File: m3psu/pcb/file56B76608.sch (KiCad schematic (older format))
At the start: 48 parts

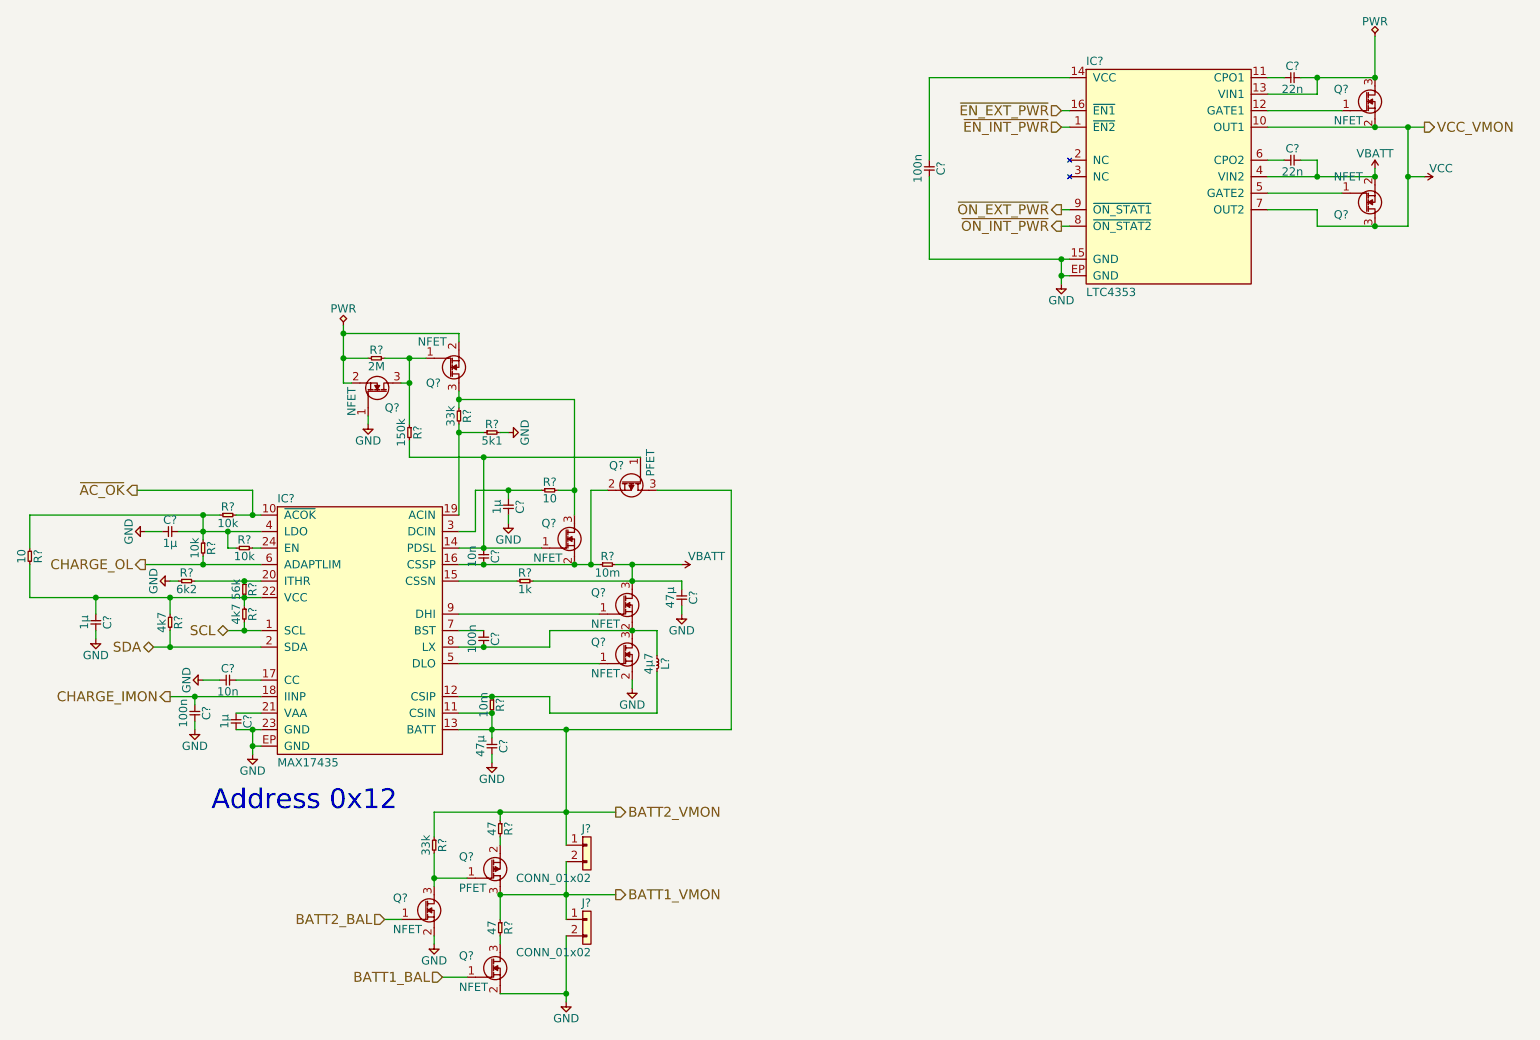
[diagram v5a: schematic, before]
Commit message: Added current monitor and control for pyros. Modified DC/DC converters.
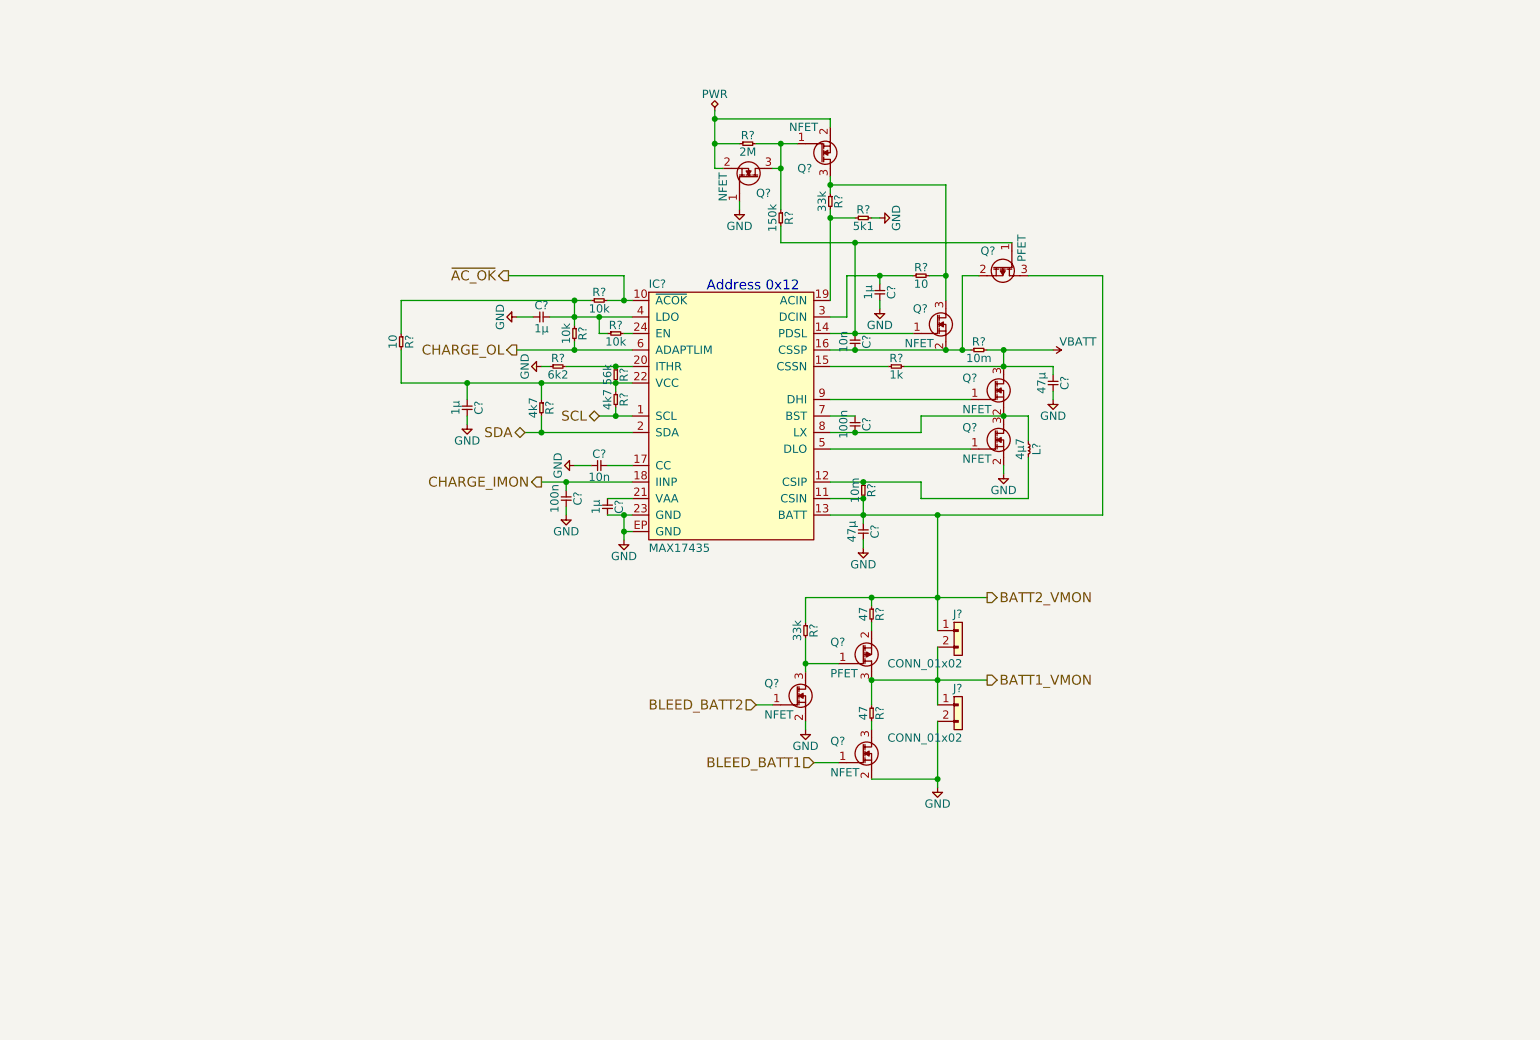
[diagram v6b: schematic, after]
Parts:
- removed C?: 100n, agg:0402, symbol C
- removed C?: 22n, ag:0402, symbol C
- removed C?: 22n, agg:0402, symbol C
- removed IC?: LTC4353, agg:DFN-16-EP-LTC-DE, symbol LTC4353
- removed Q? (x2): NFET, symbol NFET
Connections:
- net BATT1_BAL renamed BLEED_BATT1
- net BATT2_BAL renamed BLEED_BATT2
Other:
- moved on the sheet: C?, IC?, J?, L?, Q?, R?

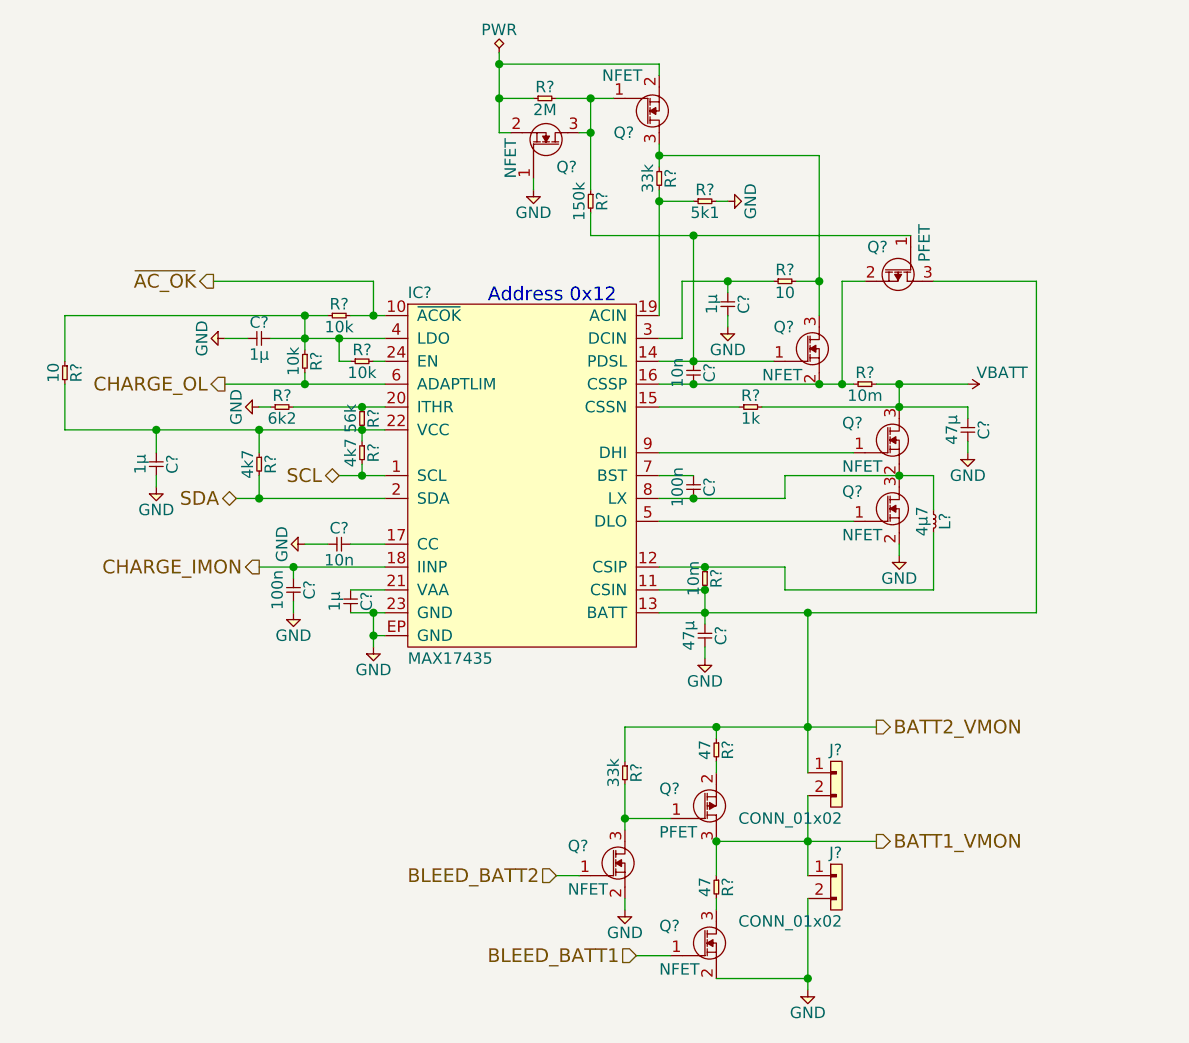
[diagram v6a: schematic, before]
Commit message: Changes in arrangement of schematic. Started wiring interconnects. WIP.
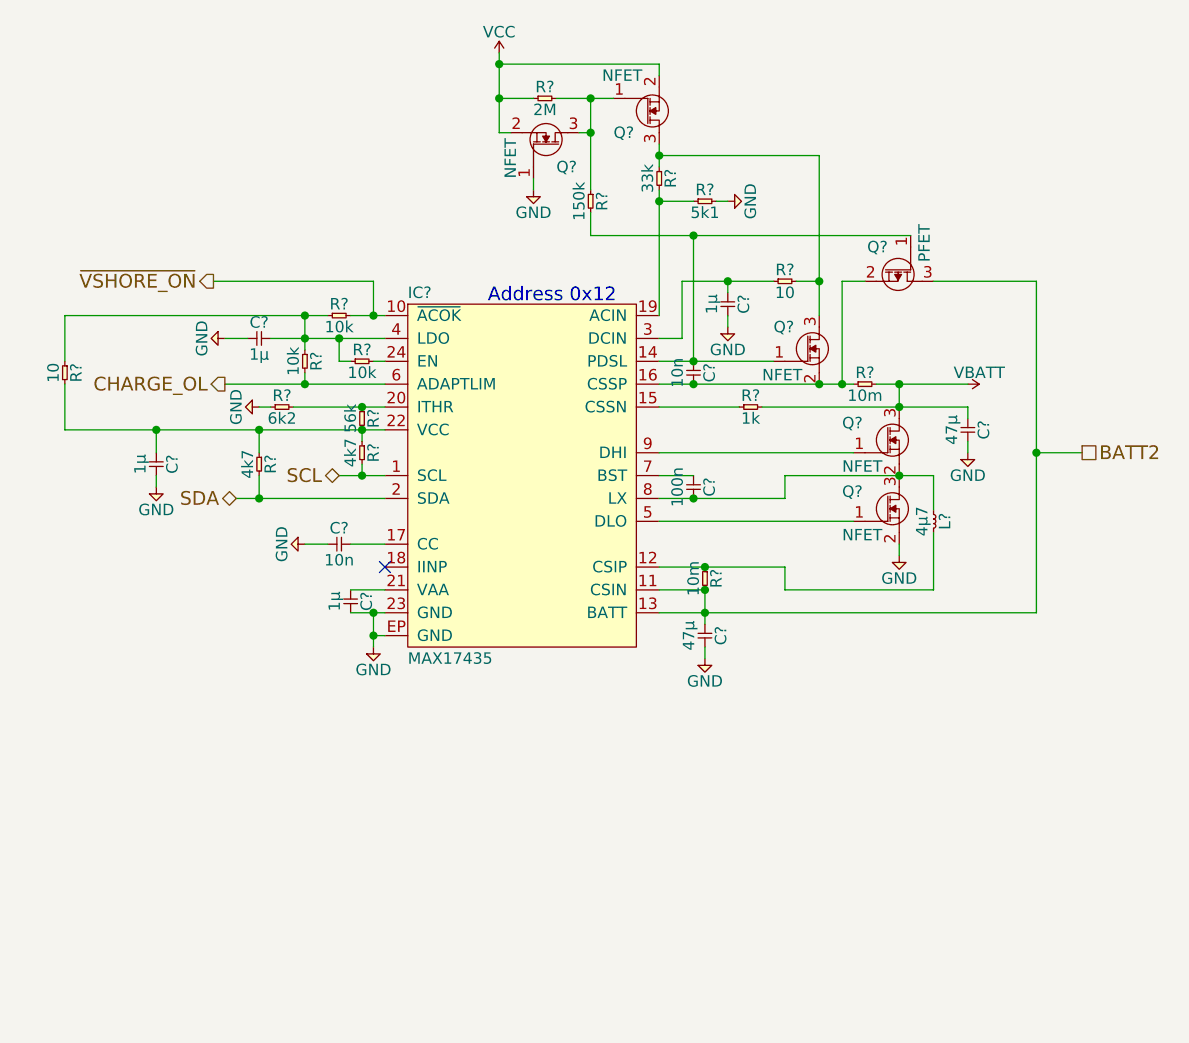
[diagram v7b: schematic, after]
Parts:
- removed C?: 100n, agg:0402, symbol C
- removed J? (x2): CONN_01x02, symbol CONN_01x02
- removed Q?: PFET, symbol PFET
- removed Q? (x2): NFET, symbol NFET
- removed R? (x2): 47, agg:0805, symbol R
- removed R?: 33k, agg:0402, symbol R
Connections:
- net VCC: now reaches Q?.2 (S), Q?.2 (S), R?.1
- net BATT2_VMON renamed BATT2
- net CHARGE_IMON: no longer names the net of IC?.18 (IINP)
- net ~AC_OK renamed ~VSHORE_ON
- no-connect marks 0 -> 1
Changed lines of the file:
@@
 $Descr A4 11693 8268
 encoding utf-8
-Sheet 3 12
+Sheet 3 13
 Title ""
 Date ""
@@
 $EndDescr
 $Comp
-L CONN_01x02 J?
-U 1 1 56B94890
-P 7200 4800
-F 0 "J?" H 7150 4900 50  0000 L CNN
-F 1 "CONN_01x02" H 7150 4600 50  0000 L CNN
-F 2 "" H 7200 4800 50  0001 C CNN
-F 3 "" H 7200 4800 50  0001 C CNN
-	1    7200 4800
-	-1   0    0    -1
-$EndComp
-$Comp
-L CONN_01x02 J?
-U 1 1 56B9491D
-P 7200 5250
-F 0 "J?" H 7150 5350 50  0000 L CNN
-F 1 "CONN_01x02" H 7150 5050 50  0000 L CNN
-F 2 "" H 7200 5250 50  0001 C CNN
-F 3 "" H 7200 5250 50  0001 C CNN
-	1    7200 5250
-	-1   0    0    -1
-$EndComp
-$Comp
 L MAX17435 IC?
 U 1 1 56B94994
@@
 $EndComp
 $Comp
-L GND #PWR08
-U 1 1 56B94BFC
-P 7100 5750
-F 0 "#PWR08" H 6970 5790 50  0001 L CNN
-F 1 "GND" H 7100 5650 50  0000 C CNN
-F 2 "" H 7100 5750 60  0000 C CNN
-F 3 "" H 7100 5750 60  0000 C CNN
-	1    7100 5750
-	1    0    0    -1
-$EndComp
-$Comp
 L R R?
 U 1 1 56B94FDE
@@
 F 4 "2210793" H 5000 3800 60  0001 C CNN "Farnell"
 	1    5000 3800
-	1    0    0    -1
-$EndComp
-$Comp
-L C C?
-U 1 1 56B99D2E
-P 4850 3950
-F 0 "C?" H 4900 4020 50  0000 C CNN
-F 1 "100n" H 4900 3880 50  0000 C CNN
-F 2 "agg:0402" H 4850 3950 50  0001 C CNN
-F 3 "" H 4850 3950 50  0001 C CNN
-F 4 "2496811" H 4850 3950 60  0001 C CNN "Farnell"
-	1    4850 3950
-	0    1    1    0
-$EndComp
-$Comp
-L GND #PWR013
-U 1 1 56B99D99
-P 4850 4100
-F 0 "#PWR013" H 4720 4140 50  0001 L CNN
-F 1 "GND" H 4850 4000 50  0000 C CNN
-F 2 "" H 4850 4100 60  0000 C CNN
-F 3 "" H 4850 4100 60  0000 C CNN
-	1    4850 4100
 	1    0    0    -1
 $EndComp
@@
 	1    0    0    -1
 $EndComp
-$Comp
-L VBATT #PWR019
-U 1 1 56C38460
-P 7800 3100
-F 0 "#PWR019" H 7800 3210 50  0001 L CNN
-F 1 "VBATT" V 7750 3250 50  0000 C CNN
-F 2 "" H 7800 3100 60  0000 C CNN
-F 3 "" H 7800 3100 60  0000 C CNN
-	1    7800 3100
-	0    1    1    0
-$EndComp
-$Comp
-L PFET Q?
-U 1 1 56C3D29E
-P 6700 4900
-F 0 "Q?" H 6450 4930 50  0000 L CNN
-F 1 "PFET" H 6450 4740 50  0000 L CNN
-F 2 "" H 6700 4900 50  0001 C CNN
-F 3 "" H 6700 4900 50  0001 C CNN
-F 4 "2335393" H 6700 4900 60  0001 C CNN "Farnell"
-	1    6700 4900
-	1    0    0    -1
-$EndComp
-$Comp
-L NFET Q?
-U 1 1 56C3D776
-P 6700 5500
-F 0 "Q?" H 6450 5530 50  0000 L CNN
-F 1 "NFET" H 6450 5340 50  0000 L CNN
-F 2 "" H 6700 5500 50  0001 C CNN
-F 3 "" H 6700 5500 50  0001 C CNN
-F 4 "2364070" H 6700 5500 60  0001 C CNN "Farnell"
-	1    6700 5500
-	1    0    0    -1
-$EndComp
 Text HLabel 4500 2650 0    60   Output ~ 0
-~AC_OK
+~VSHORE_ON
 Text HLabel 4550 3100 0    60   Output ~ 0
 CHARGE_OL
-Text HLabel 4700 3900 0    60   Output ~ 0
-CHARGE_IMON
 Text HLabel 5050 3500 0    60   BiDi ~ 0
 SCL
 Text HLabel 4600 3600 0    60   BiDi ~ 0
 SDA
-$Comp
-L R R?
-U 1 1 56C428FC
-P 6700 4650
-F 0 "R?" H 6750 4700 50  0000 C CNN
-F 1 "47" H 6750 4600 50  0000 C CNN
-F 2 "agg:0805" H 6700 4650 50  0001 C CNN
-F 3 "" H 6700 4650 50  0001 C CNN
-F 4 "1750737" H 6700 4650 60  0001 C CNN "Farnell"
-F 5 "0.5W" H 6700 4650 60  0001 C CNN "Power"
-	1    6700 4650
-	0    1    1    0
-$EndComp
-$Comp
-L R R?
-U 1 1 56C429C6
-P 6700 5250
-F 0 "R?" H 6750 5300 50  0000 C CNN
-F 1 "47" H 6750 5200 50  0000 C CNN
-F 2 "agg:0805" H 6700 5250 50  0001 C CNN
-F 3 "" H 6700 5250 50  0001 C CNN
-F 4 "1750737" H 6700 5250 60  0001 C CNN "Farnell"
-F 5 "0.5W" H 6700 5250 60  0001 C CNN "Power"
-	1    6700 5250
-	0    1    1    0
-$EndComp
-Text HLabel 6350 5600 0    60   Input ~ 0
-BLEED_BATT1
-Text HLabel 7400 5100 2    60   Output ~ 0
-BATT1_VMON
-Text HLabel 7400 4600 2    60   Output ~ 0
-BATT2_VMON
-$Comp
-L NFET Q?
-U 1 1 56C4464A
-P 6300 5150
-F 0 "Q?" H 6050 5180 50  0000 L CNN
-F 1 "NFET" H 6050 4990 50  0000 L CNN
-F 2 "" H 6300 5150 50  0001 C CNN
-F 3 "" H 6300 5150 50  0001 C CNN
-F 4 "2364070" H 6300 5150 60  0001 C CNN "Farnell"
-	1    6300 5150
-	1    0    0    -1
-$EndComp
-$Comp
-L GND #PWR020
-U 1 1 56C4477F
-P 6300 5400
-F 0 "#PWR020" H 6170 5440 50  0001 L CNN
-F 1 "GND" H 6300 5300 50  0000 C CNN
-F 2 "" H 6300 5400 60  0000 C CNN
-F 3 "" H 6300 5400 60  0000 C CNN
-	1    6300 5400
-	1    0    0    -1
-$EndComp
-$Comp
-L R R?
-U 1 1 56C44E02
-P 6300 4750
-F 0 "R?" H 6350 4800 50  0000 C CNN
-F 1 "33k" H 6350 4700 50  0000 C CNN
-F 2 "agg:0402" H 6300 4750 50  0001 C CNN
-F 3 "" H 6300 4750 50  0001 C CNN
-F 4 "2447160" H 6300 4750 60  0001 C CNN "Farnell"
-	1    6300 4750
-	0    1    1    0
-$EndComp
-Text HLabel 6000 5250 0    60   Input ~ 0
-BLEED_BATT2
-$Comp
-L PWR #FLG024
-U 1 1 56C61BF6
-P 5750 1650
-F 0 "#FLG024" H 5750 1810 50  0001 C CNN
-F 1 "PWR" H 5750 1750 50  0000 C CNN
-F 2 "" H 5750 1650 50  0001 C CNN
-F 3 "" H 5750 1650 50  0001 C CNN
-	1    5750 1650
-	1    0    0    -1
-$EndComp
+Text HLabel 8300 3400 2    60   UnSpc ~ 0
+BATT2
 $Comp
 L NFET Q?
@@
 Wire Wire Line
 	7250 2650 7350 2650
-Connection ~ 7100 4100
 Wire Wire Line
 	8100 4100 8100 2650
@@
 Connection ~ 5750 1700
 Wire Wire Line
-	6700 4650 6700 4600
-Wire Wire Line
-	7100 4100 7100 4800
-Wire Wire Line
 	6750 2650 6750 2700
 Wire Wire Line
@@
 	5150 3450 5150 3500
 Connection ~ 6600 3600
-Wire Wire Line
-	6100 5250 6000 5250
-Connection ~ 6300 5000
-Connection ~ 6700 4600
-Wire Wire Line
-	6300 4600 6300 4750
-Wire Wire Line
-	6300 4850 6300 5050
-Wire Wire Line
-	6300 5000 6500 5000
-Wire Wire Line
-	6300 5350 6300 5400
-Connection ~ 6700 5100
-Wire Wire Line
-	6700 4750 6700 4800
-Wire Wire Line
-	6500 5600 6350 5600
-Wire Wire Line
-	6700 5250 6700 5100
-Wire Wire Line
-	6700 5350 6700 5400
-Connection ~ 7100 5700
-Wire Wire Line
-	6700 5700 7100 5700
 Wire Wire Line
 	4250 3300 4250 3400
@@
 Connection ~ 4700 3600
 Connection ~ 5150 3500
-Connection ~ 7100 5100
-Wire Wire Line
-	6700 5100 7400 5100
-Connection ~ 7100 4600
-Wire Wire Line
-	6300 4600 7400 4600
-Wire Wire Line
-	7100 5350 7100 5750
-Wire Wire Line
-	7100 4900 7100 5250
 Connection ~ 7500 3100
 Wire Wire Line
@@
 Connection ~ 5050 2900
 Wire Wire Line
-	5050 3000 5050 2900
+	5050 2900 5050 3000
 Wire Wire Line
 	5200 3000 5250 3000
@@
 	4250 3500 4250 3550
 Connection ~ 4900 2800
-Wire Wire Line
-	4850 4050 4850 4100
-Connection ~ 4850 3900
-Wire Wire Line
-	4850 3950 4850 3900
-Wire Wire Line
-	4700 3900 5250 3900
 Connection ~ 5200 4200
 Connection ~ 5200 4100
@@
 Text Notes 5700 2750 0    60   ~ 0
 Address 0x12
+NoConn ~ 5250 3900
+$Comp
+L VCC #PWR?
+U 1 1 56E18C4B
+P 5750 1650
+F 0 "#PWR?" H 5750 1760 50  0001 L CNN
+F 1 "VCC" H 5750 1740 50  0000 C CNN
+F 2 "" H 5750 1650 60  0000 C CNN
+F 3 "" H 5750 1650 60  0000 C CNN
+	1    5750 1650
+	1    0    0    -1
+$EndComp
+$Comp
+L VBATT #PWR?
+U 1 1 56E1ABD5
+P 7800 3100
+F 0 "#PWR?" H 7800 3210 50  0001 L CNN
+F 1 "VBATT" V 7750 3150 50  0000 C CNN
+F 2 "" H 7800 3100 60  0000 C CNN
+F 3 "" H 7800 3100 60  0000 C CNN
+	1    7800 3100
+	0    1    1    0
+$EndComp
+Wire Wire Line
+	8300 3400 8100 3400
+Connection ~ 8100 3400
 $EndSCHEMATC
